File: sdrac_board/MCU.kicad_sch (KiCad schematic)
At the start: 38 parts, among them J1 INOUT, J11 SYNCHRONIZER, J12 SWD, SW1 BOOT0, SW2 NRST, SW3 USR_BTN, U1 FM24CL16B, U2 STM32F412RGT6, Y1 16MHz

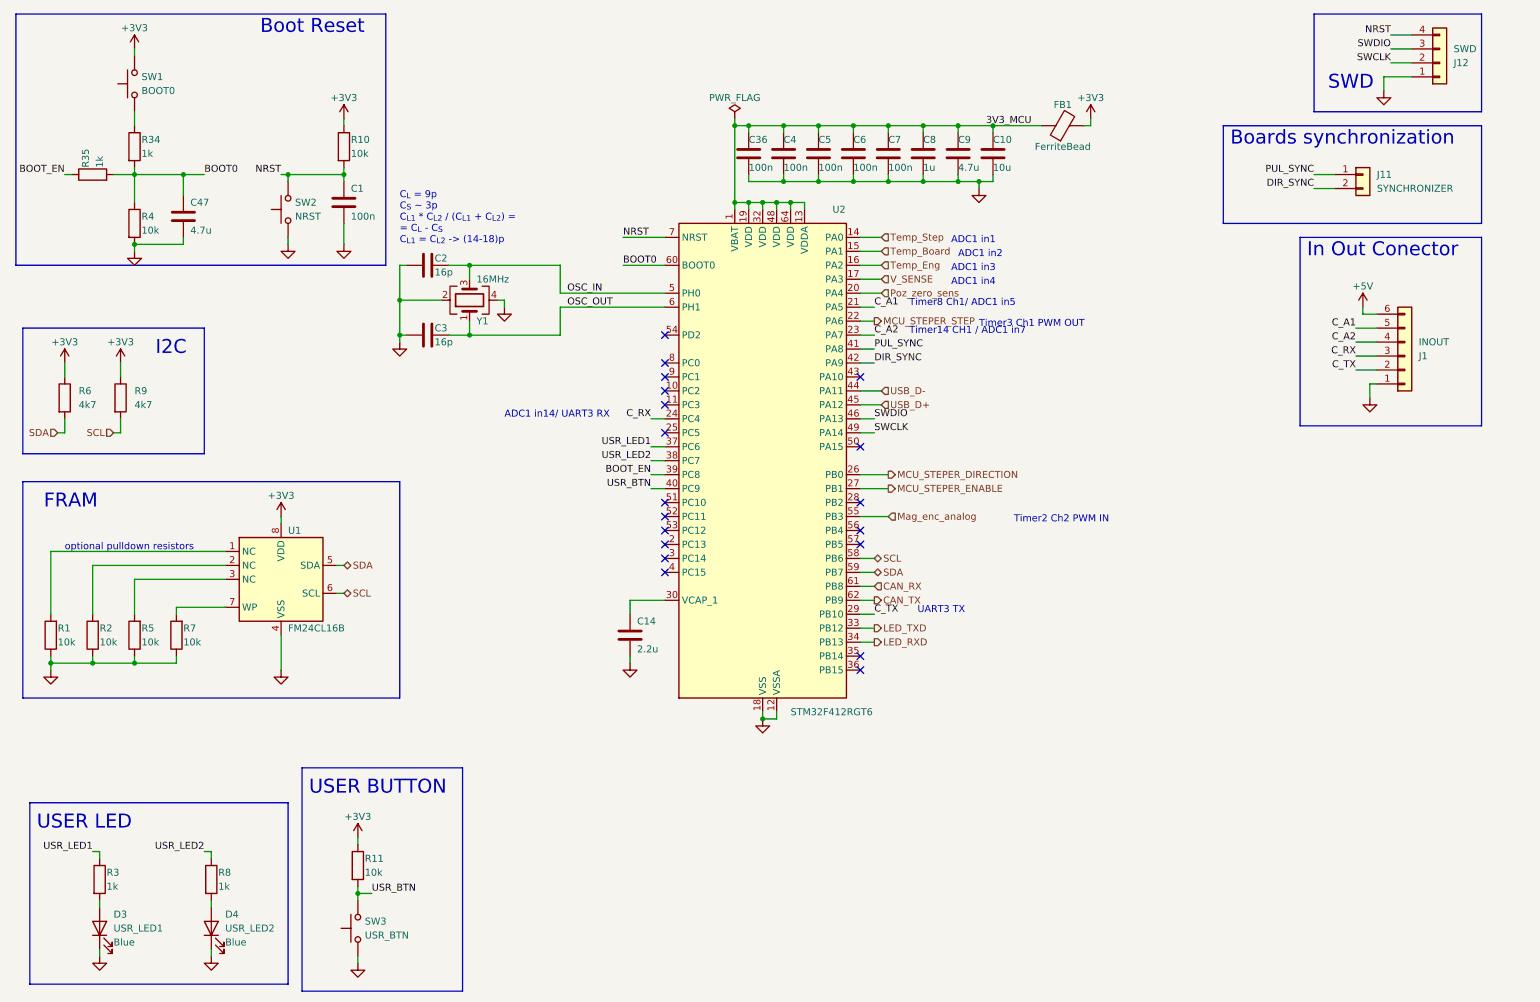
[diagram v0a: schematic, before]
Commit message: added second I2C communscation lane for synchronization and added wyas to change mcirosteping with resistors
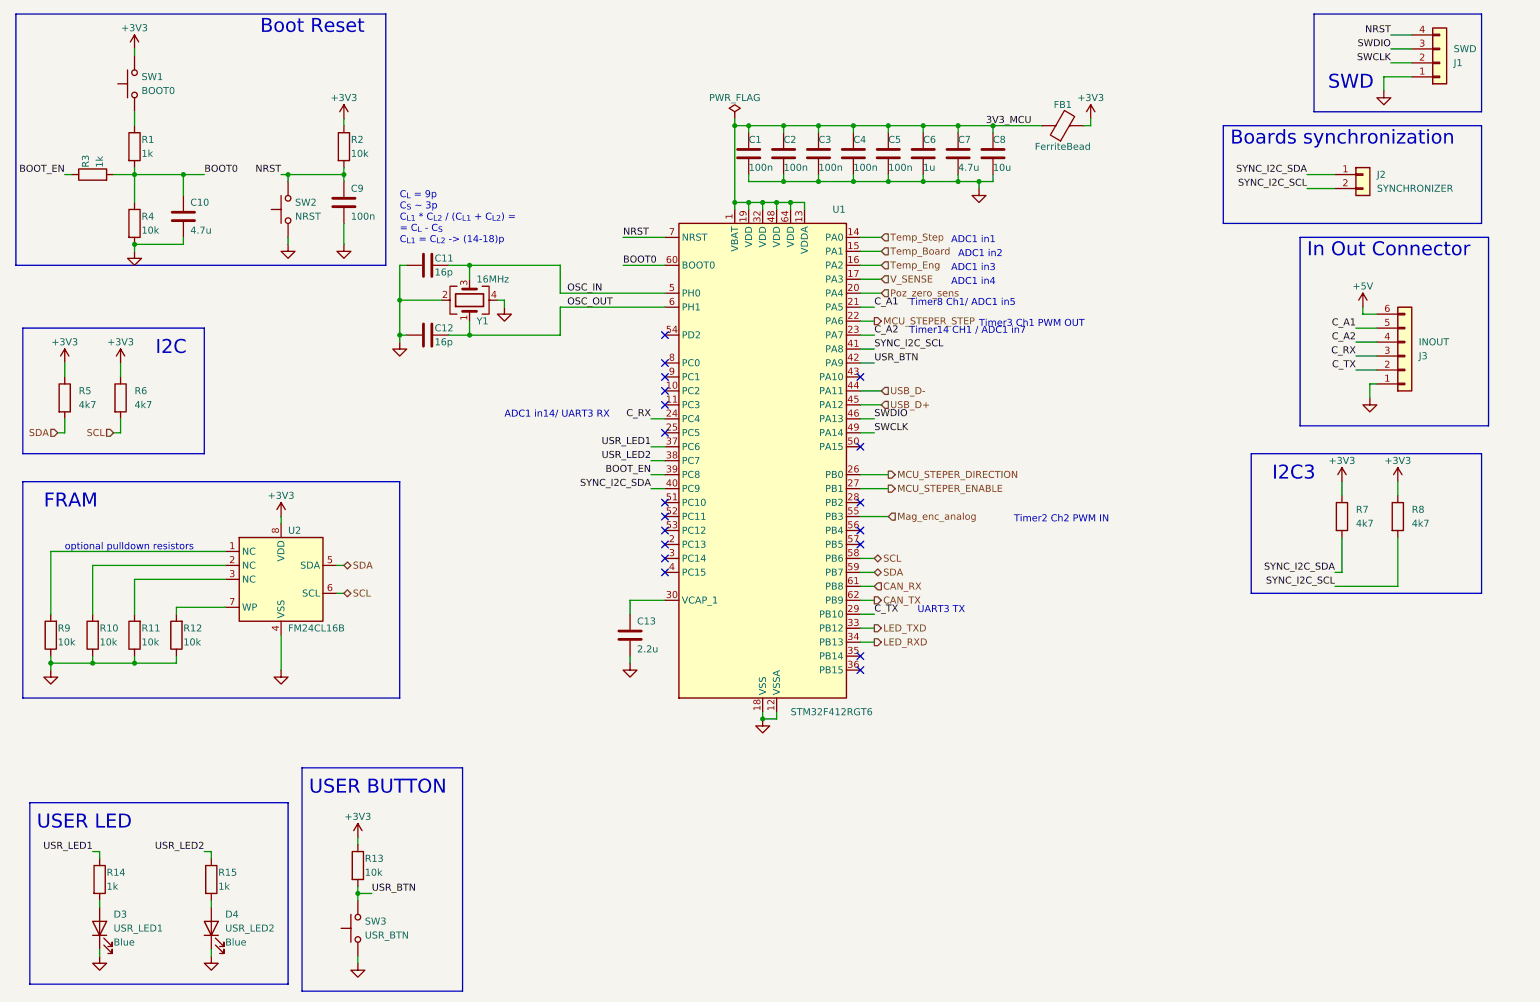
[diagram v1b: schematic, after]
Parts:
- added R7, R8: 4k7, Resistor_SMD:R_0402_1005Metric, symbol Device:R
- renumbered C36 to C1, C47 to C10, C2 to C11, C3 to C12, C14 to C13, C4 to C2, C5 to C3, C6 to C4, C7 to C5, C8 to C6, C9 to C7, C10 to C8, C1 to C9, J12 to J1, J11 to J2, J1 to J3, R34 to R1, R2 to R10, R5 to R11, R7 to R12, R11 to R13, R3 to R14, R8 to R15, R10 to R2, R35 to R3, R6 to R5, R9 to R6, R1 to R9, U2 to U1, U1 to U2
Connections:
- net +3V3: now also R7.1, R8.1
- net USR_BTN: now also U1.42 (PA9); no longer U1.40 (PC9)
- net DIR_SYNC renamed SYNC_I2C_SCL
- net SYNC_I2C_SCL: now also U1.41 (PA8), R8.2; no longer U1.42 (PA9)
- net PUL_SYNC renamed SYNC_I2C_SDA
- net SYNC_I2C_SDA: now also U1.40 (PC9), R7.2; no longer U1.41 (PA8)
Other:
- note added: "I2C3"
- note added: "In Out Connector"
- note removed: "In Out Conector"

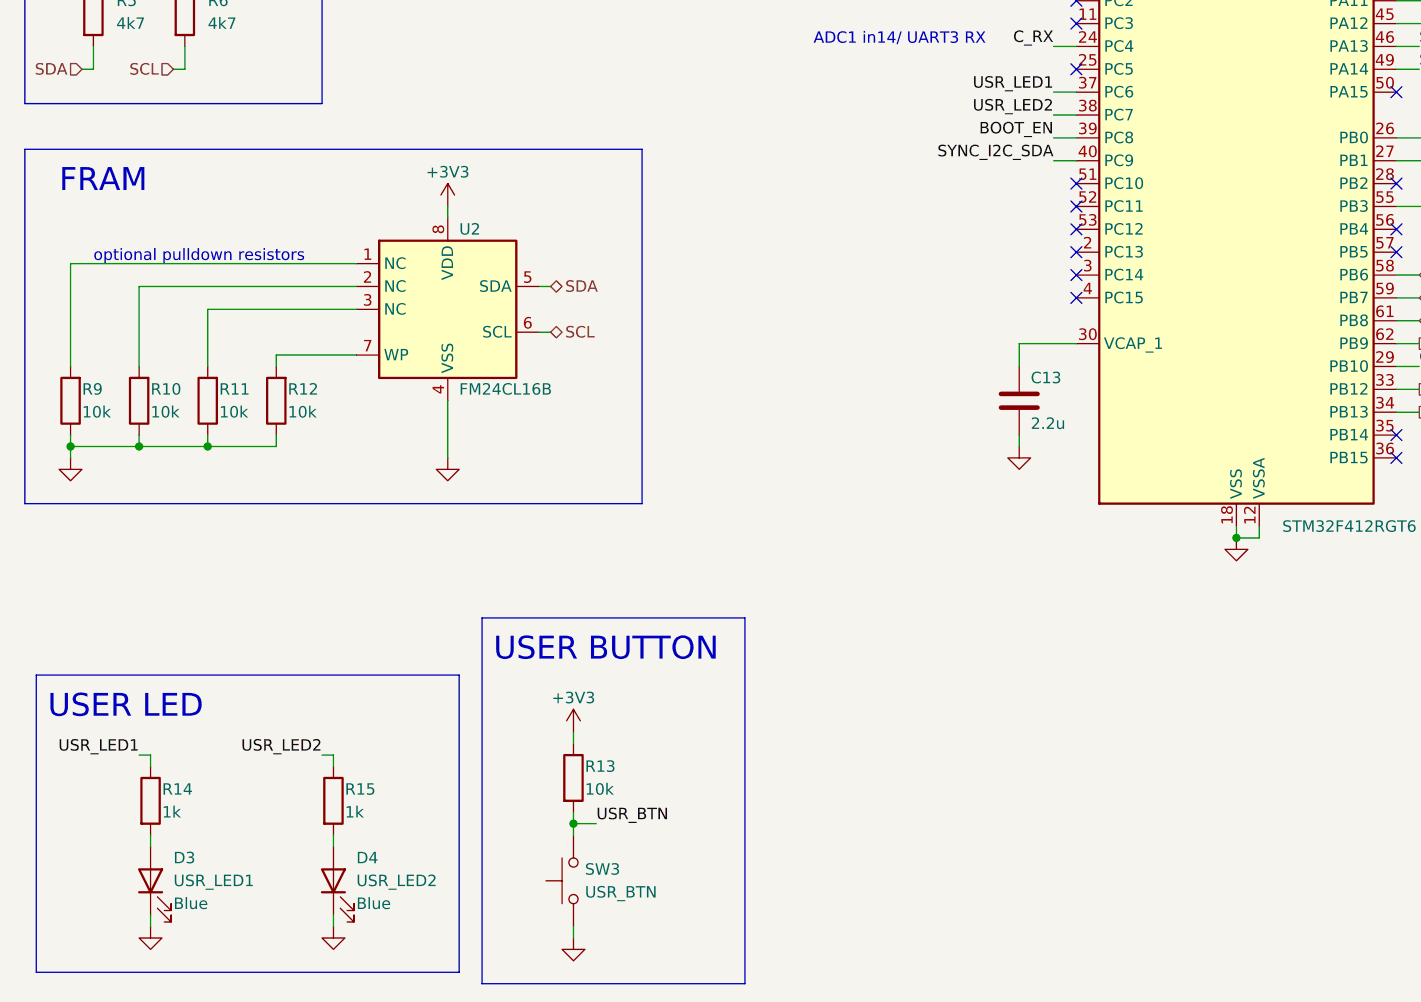
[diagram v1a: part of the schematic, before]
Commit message: added hardware address selector
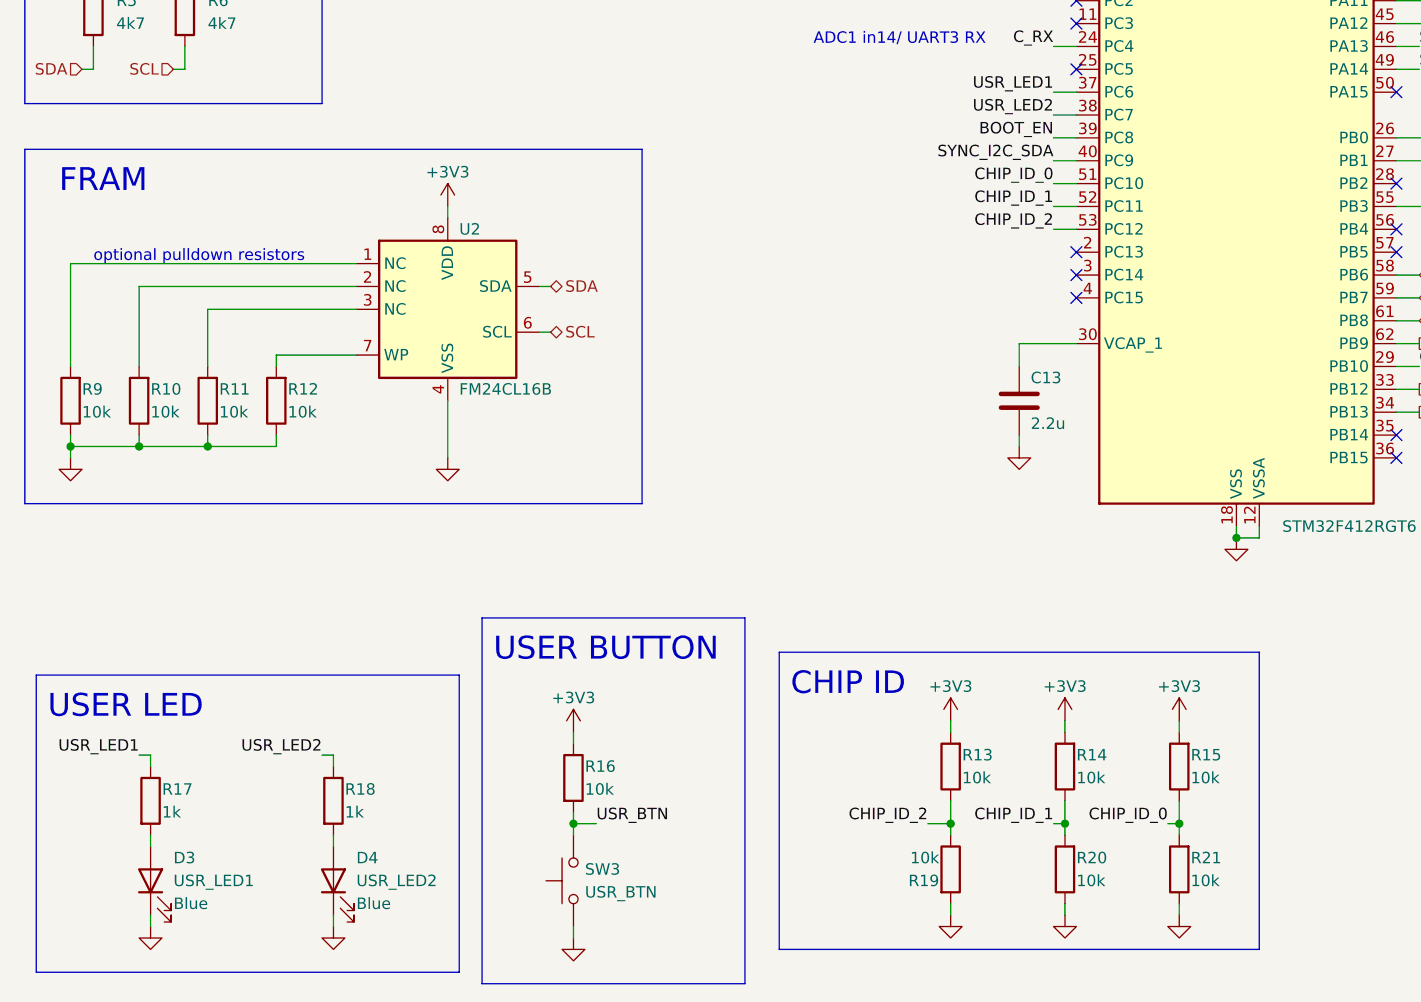
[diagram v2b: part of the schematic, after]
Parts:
- added R13, R14, R15, R19, R20, R21: 10k, Resistor_SMD:R_0402_1005Metric, symbol Device:R
- renumbered R13 to R16, R14 to R17, R15 to R18
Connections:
- net +3V3: now also R13.2, R14.2, R15.2
- net GND: now also R19.2, R20.1, R21.1
- net CHIP_ID_0: now reaches U1.51 (PC10)
- net CHIP_ID_0: now also R15.1, R21.2
- net CHIP_ID_1: now reaches U1.52 (PC11)
- net CHIP_ID_1: now also R14.1, R20.2
- net CHIP_ID_2: now reaches U1.53 (PC12)
- net CHIP_ID_2: now also R13.1, R19.1
- no-connect marks 19 -> 16
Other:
- note added: "CHIP ID"
